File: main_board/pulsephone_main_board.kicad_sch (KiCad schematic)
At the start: 44 parts, among them J1 USB_C_Receptacle_USB2.0_14P, J2 Conn_01x05, J3 Conn_2Rows-35Pins_MountingPin, J4 Conn_2Rows-35Pins_MountingPin, J5 Conn_2Rows-35Pins_MountingPin, SW1 SW_DPST_x2, U1 XL1509-3.3, U2 PCM5102APWR, U5 TP4056-42-ESOP8

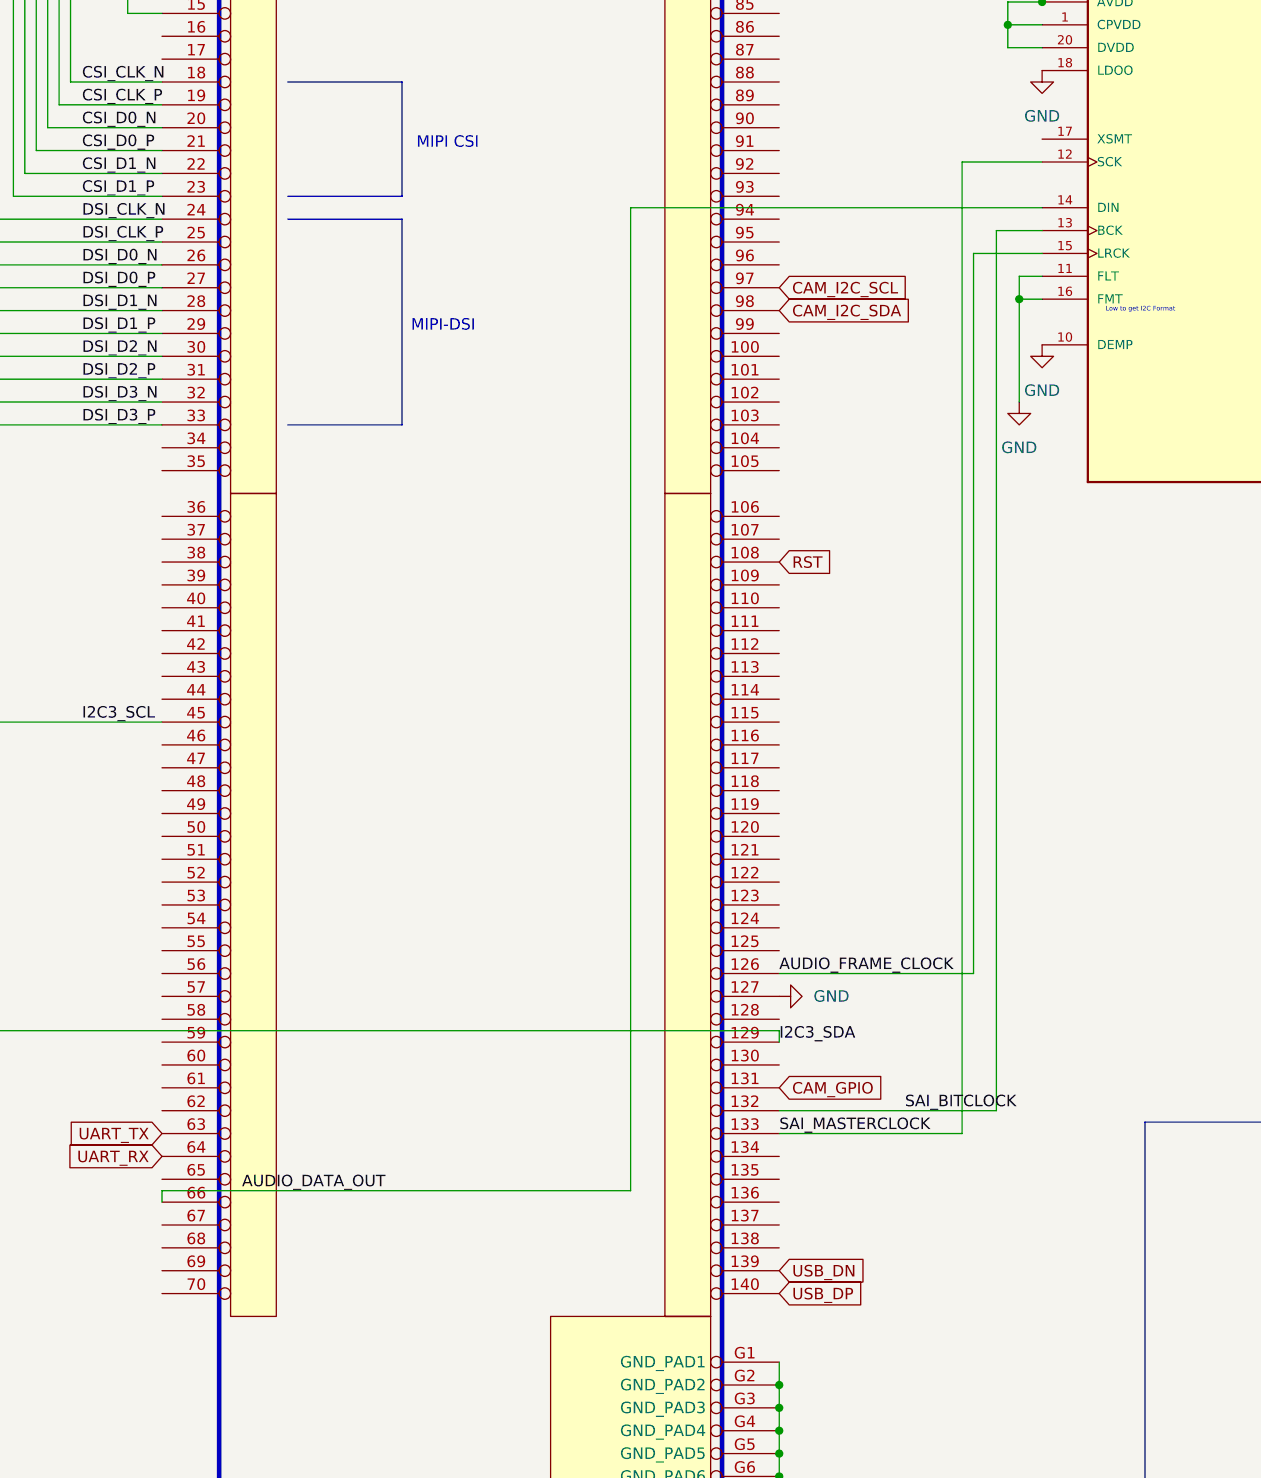
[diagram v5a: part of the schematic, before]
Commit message: rewire traces for new connector scheme
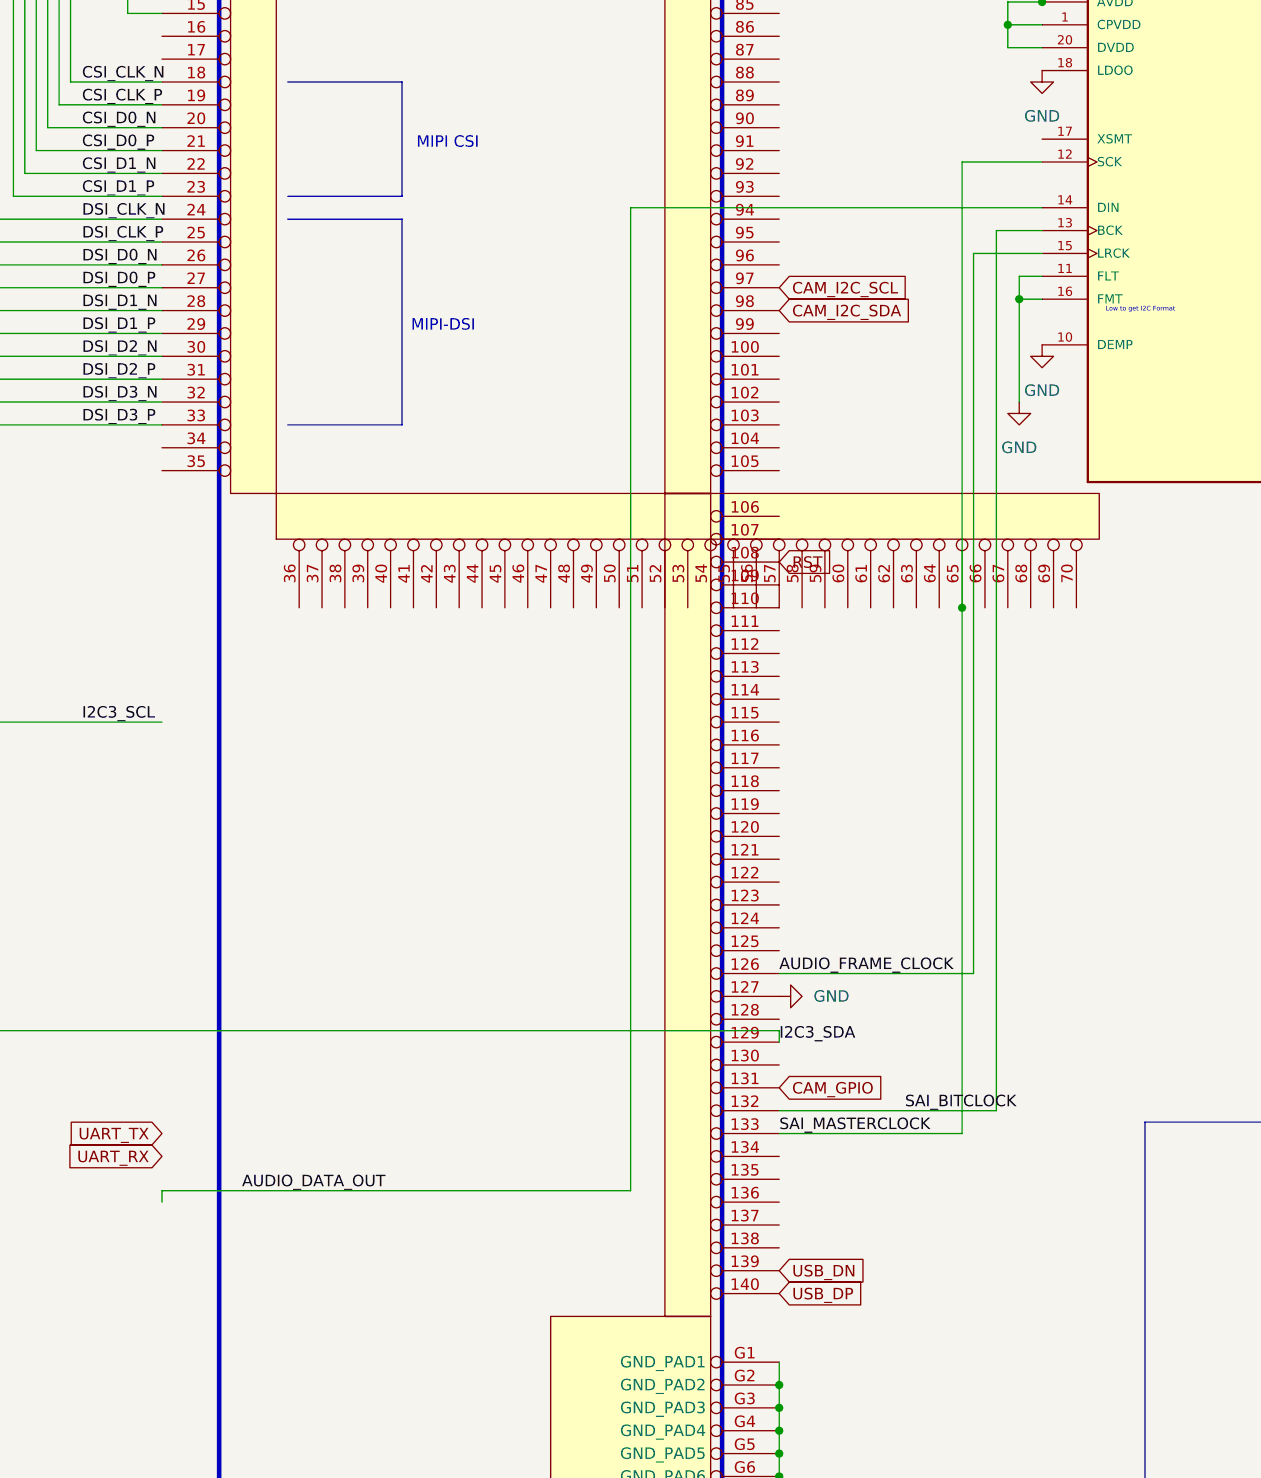
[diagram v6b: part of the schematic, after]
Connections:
- net AUDIO_DATA_OUT: no longer MCM93_MOD1.66 (31)
- net I2C3_SCL: no longer MCM93_MOD1.45 (10)
- net SAI_MASTERCLOCK: now also MCM93_MOD1.65 (30)
- net UART_RX: no longer MCM93_MOD1.64 (29)
- net UART_TX: no longer MCM93_MOD1.63 (28)
- net at MCM93_MOD1.110 (5): now also MCM93_MOD1.57 (22)
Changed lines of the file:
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@@
 	)
 	(junction
+		(at 449.58 264.16)
+		(diameter 0)
+		(color 0 0 0 0)
+	)
+	(junction
 		(at 661.67 386.08)
 		(diameter 0)
@@
 	(wire
 		(pts
-			(xy 449.58 214.63) (xy 449.58 322.58)
+			(xy 449.58 214.63) (xy 449.58 264.16)
 		)
 		(stroke
@@
 	(wire
 		(pts
+			(xy 449.58 264.16) (xy 449.58 322.58)
+		)
+		(stroke
+			(width 0)
+			(type default)
+		)
+	)
+	(wire
+		(pts
 			(xy 349.25 118.11) (xy 299.72 118.11)
 		)
@@
 	(symbol
 		(lib_id "mcm-imx93:MCM93_MOD")
-		(at 373.38 251.46 0)
-		(mirror y)
+		(at 373.38 251.46 90)
+		(mirror x)
 		(unit 2)
 		(exclude_from_sim no)
@@
 		(dnp no)
 		(property "Reference" "MCM93_MOD1"
-			(at 370.84 248.92 0)
+			(at 370.84 254 0)
 			(effects
 				(font
@@
 		)
 		(property "Value" "MCM93_MOD"
-			(at 373.38 345.44 0)
+			(at 467.36 251.46 0)
 			(effects
 				(font
@@
 		)
 		(property "Part Reference" ""
-			(at 373.38 332.74 0)
+			(at 454.66 251.46 0)
 			(effects
 				(font
@@
 		)
 		(property "ALTIUM_VALUE" ""
-			(at 373.38 332.74 0)
+			(at 454.66 251.46 0)
 			(effects
 				(font

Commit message: fix some errors
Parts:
- added R4: 1.2 kΩ, Resistor_SMD:R_0805_2012Metric, symbol Device:R
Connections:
- net AUDIO_DATA_OUT: now also MCM93_MOD1.66 (31)
- net GND: now also R4.2
- net I2C3_SCL: now also MCM93_MOD1.45 (10)
- net SAI_MASTERCLOCK: no longer MCM93_MOD1.65 (30)
- net UART_RX: now also MCM93_MOD1.64 (29)
- net UART_TX: now also MCM93_MOD1.63 (28)
- net at MCM93_MOD1.110 (5): no longer MCM93_MOD1.57 (22)
- net at U5.2 (PROG): now also R4.1
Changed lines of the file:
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@@
 	)
 	(junction
-		(at 449.58 264.16)
-		(diameter 0)
-		(color 0 0 0 0)
-	)
-	(junction
 		(at 661.67 386.08)
 		(diameter 0)
@@
 	)
 	(junction
-		(at 577.85 364.49)
-		(diameter 0)
-		(color 0 0 0 0)
-	)
-	(junction
 		(at 635 405.13)
 		(diameter 0)
@@
 	(wire
 		(pts
-			(xy 665.48 405.13) (xy 665.48 414.02)
+			(xy 661.67 405.13) (xy 661.67 414.02)
 		)
 		(stroke
@@
 	(wire
 		(pts
+			(xy 320.04 217.17) (xy 320.04 241.3)
+		)
+		(stroke
+			(width 0)
+			(type default)
+		)
+	)
+	(wire
+		(pts
 			(xy 429.26 403.86) (xy 429.26 406.4)
 		)
@@
 		)
 	)
-	(wire
-		(pts
-			(xy 577.85 364.49) (xy 579.12 364.49)
-		)
-		(stroke
-			(width 0)
-			(type default)
-		)
-	)
 	(polyline
 		(pts
@@
 	(wire
 		(pts
-			(xy 317.5 311.15) (xy 317.5 223.52)
+			(xy 317.5 223.52) (xy 317.5 311.15)
 		)
 		(stroke
@@
 	(wire
 		(pts
-			(xy 661.67 405.13) (xy 665.48 405.13)
-		)
-		(stroke
-			(width 0)
-			(type default)
-		)
-	)
-	(wire
-		(pts
 			(xy 567.69 415.29) (xy 574.04 415.29)
 		)
@@
 	(wire
 		(pts
+			(xy 661.67 421.64) (xy 665.48 421.64)
+		)
+		(stroke
+			(width 0)
+			(type default)
+		)
+	)
+	(wire
+		(pts
 			(xy 689.61 344.17) (xy 706.12 344.17)
 		)
@@
 	(wire
 		(pts
-			(xy 320.04 241.3) (xy 320.04 217.17)
-		)
-		(stroke
-			(width 0)
-			(type default)
-		)
-	)
-	(wire
-		(pts
 			(xy 346.71 213.36) (xy 360.68 213.36)
 		)
@@
 	(wire
 		(pts
-			(xy 449.58 214.63) (xy 449.58 264.16)
+			(xy 449.58 214.63) (xy 449.58 322.58)
 		)
 		(stroke
@@
 	(wire
 		(pts
-			(xy 449.58 264.16) (xy 449.58 322.58)
-		)
-		(stroke
-			(width 0)
-			(type default)
-		)
-	)
-	(wire
-		(pts
 			(xy 349.25 118.11) (xy 299.72 118.11)
 		)
@@
 	)
 	(symbol
+		(lib_name "GND_1")
+		(lib_id "power:GND")
+		(at 665.48 421.64 0)
+		(unit 1)
+		(exclude_from_sim no)
+		(in_bom yes)
+		(on_board yes)
+		(dnp no)
+		(property "Reference" "#PWR072"
+			(at 665.48 427.99 0)
+			(effects
+				(font
+					(size 1.27 1.27)
+				)
+				(hide yes)
+			)
+		)
+		(property "Value" "GND"
+			(at 665.48 426.72 0)
+			(effects
+				(font
+					(size 1.27 1.27)
+				)
+			)
+		)
+		(property "Footprint" ""
+			(at 665.48 421.64 0)
+			(effects
+				(font
+					(size 1.27 1.27)
+				)
+				(hide yes)
+			)
+		)
+		(property "Datasheet" ""
+			(at 665.48 421.64 0)
+			(effects
+				(font
+					(size 1.27 1.27)
+				)
+				(hide yes)
+			)
+		)
+		(property "Description" "Power symbol creates a global label with name \"GND\" , ground"
+			(at 665.48 421.64 0)
+			(effects
+				(font
+					(size 1.27 1.27)
+				)
+				(hide yes)
+			)
+		)
+		(pin "1"
+		)
+		(instances
+			(project "pulsephone_main_board"
+				(path "/95397744-6eff-4b94-a4c8-db9ebac7d828"
+					(reference "#PWR072")
+					(unit 1)
+				)
+			)
+		)
+	)
+	(symbol
 		(lib_id "Mechanical:MountingHole")
 		(at 660.4 198.12 0)
@@
 	)
 	(symbol
+		(lib_id "Device:R")
+		(at 661.67 417.83 0)
+		(unit 1)
+		(exclude_from_sim no)
+		(in_bom yes)
+		(on_board yes)
+		(dnp no)
+		(property "Reference" "R4"
+			(at 664.21 416.5599 0)
+			(effects
+				(font
+					(size 1.27 1.27)
+				)
+				(justify left)
+			)
+		)
+		(property "Value" "1.2 kΩ"
+			(at 656.844 423.164 0)
+			(effects
+				(font
+					(size 1.27 1.27)
+				)
+				(justify left)
+			)
+		)
+		(property "Footprint" "Resistor_SMD:R_0805_2012Metric"
+			(at 659.892 417.83 90)
+			(effects
+				(font
+					(size 1.27 1.27)
+				)
+				(hide yes)
+			)
+		)
+		(property "Datasheet" "~"
+			(at 661.67 417.83 0)
+			(effects
+				(font
+					(size 1.27 1.27)
+				)
+				(hide yes)
+			)
+		)
+		(property "Description" "Resistor"
+			(at 661.67 417.83 0)
+			(effects
+				(font
+					(size 1.27 1.27)
+				)
+				(hide yes)
+			)
+		)
+		(pin "2"
+		)
+		(pin "1"
+		)
+		(instances
+			(project "pulsephone_main_board"
+				(path "/95397744-6eff-4b94-a4c8-db9ebac7d828"
+					(reference "R4")
+					(unit 1)
+				)
+			)
+		)
+	)
+	(symbol
 		(lib_id "power:+3.3V")
 		(at 510.54 359.41 90)
@@
 	(symbol
 		(lib_id "mcm-imx93:MCM93_MOD")
-		(at 373.38 251.46 90)
-		(mirror x)
+		(at 373.38 251.46 0)
+		(mirror y)
 		(unit 2)
 		(exclude_from_sim no)
@@
 		(dnp no)
 		(property "Reference" "MCM93_MOD1"
-			(at 370.84 254 0)
+			(at 370.84 248.92 0)
 			(effects
 				(font
@@
 		)
 		(property "Value" "MCM93_MOD"
-			(at 467.36 251.46 0)
+			(at 373.38 345.44 0)
 			(effects
 				(font
@@
 		)
 		(property "Part Reference" ""
-			(at 454.66 251.46 0)
+			(at 373.38 332.74 0)
 			(effects
 				(font
@@
 		)
 		(property "ALTIUM_VALUE" ""
-			(at 454.66 251.46 0)
+			(at 373.38 332.74 0)
 			(effects
 				(font

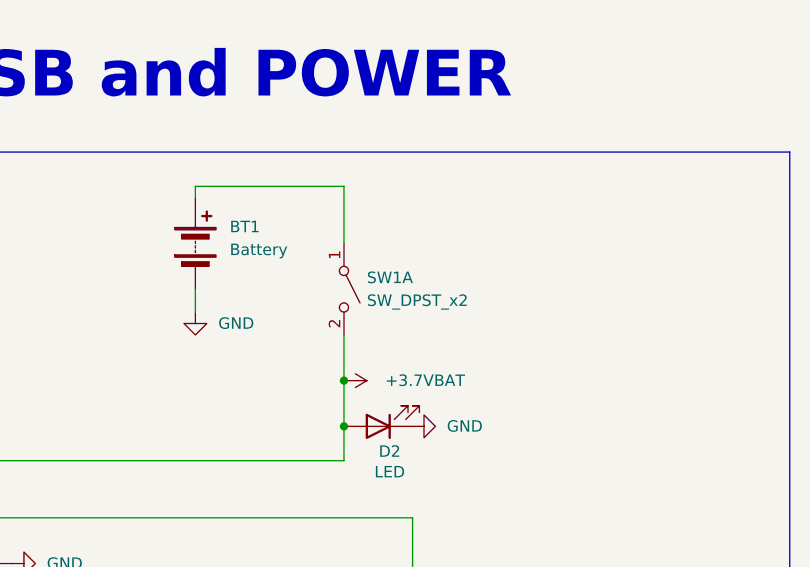
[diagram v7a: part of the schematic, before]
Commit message: remove battery switch
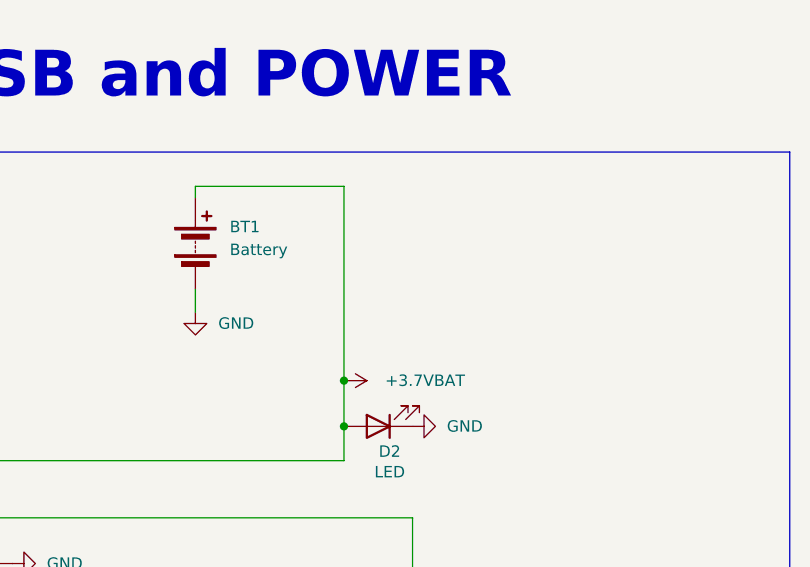
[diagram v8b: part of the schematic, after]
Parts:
- removed SW1: SW_DPST_x2, Button_Switch_SMD:SW_Tactile_SPST_NO_Straight_CK_PTS636Sx25SMTRLFS, symbol Switch:SW_DPST_x2
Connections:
- net +3.7VBAT: now also BT1.1 (+)
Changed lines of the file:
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@@
 	(wire
 		(pts
+			(xy 706.12 344.17) (xy 706.12 365.76)
+		)
+		(stroke
+			(width 0)
+			(type default)
+		)
+	)
+	(wire
+		(pts
 			(xy 511.81 407.67) (xy 521.97 407.67)
 		)
@@
 	(wire
 		(pts
-			(xy 706.12 344.17) (xy 706.12 350.52)
-		)
-		(stroke
-			(width 0)
-			(type default)
-		)
-	)
-	(wire
-		(pts
 			(xy 429.26 391.16) (xy 429.26 393.7)
 		)
@@
 	(wire
 		(pts
-			(xy 706.12 360.68) (xy 706.12 365.76)
-		)
-		(stroke
-			(width 0)
-			(type default)
-		)
-	)
-	(wire
-		(pts
 			(xy 723.9 411.48) (xy 723.9 410.21)
 		)
@@
 					(unit 1)
 				)
-			)
-		)
-	)
-	(symbol
-		(lib_id "Switch:SW_DPST_x2")
-		(at 706.12 355.6 270)
-		(unit 1)
-		(exclude_from_sim no)
-		(in_bom yes)
-		(on_board yes)
-		(dnp no)
-		(fields_autoplaced yes)
-		(property "Reference" "SW1"
-			(at 708.66 354.3299 90)
-			(effects
-				(font
-					(size 1.27 1.27)
-				)
-				(justify left)
-			)
-		)
-		(property "Value" "SW_DPST_x2"
-			(at 708.66 356.8699 90)
-			(effects
-				(font
-					(size 1.27 1.27)
-				)
-				(justify left)
-			)
-		)
-		(property "Footprint" "Button_Switch_SMD:SW_Tactile_SPST_NO_Straight_CK_PTS636Sx25SMTRLFS"
-			(at 706.12 355.6 0)
-			(effects
-				(font
-					(size 1.27 1.27)
-				)
-				(hide yes)
-			)
-		)
-		(property "Datasheet" "~"
-			(at 706.12 355.6 0)
-			(effects
-				(font
-					(size 1.27 1.27)
-				)
-				(hide yes)
-			)
-		)
-		(property "Description" "Single Pole Single Throw (SPST) switch, separate symbol"
-			(at 706.12 355.6 0)
-			(effects
-				(font
-					(size 1.27 1.27)
-				)
-				(hide yes)
-			)
-		)
-		(pin "4"
-		)
-		(pin "1"
-		)
-		(pin "2"
-		)
-		(pin "3"
-		)
-		(instances
-			(project ""
-				(path "/95397744-6eff-4b94-a4c8-db9ebac7d828"
-					(reference "SW1")
-					(unit 1)
-				)
